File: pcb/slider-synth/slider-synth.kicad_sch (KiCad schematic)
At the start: 21 parts, among them J1 USB4105, J2 PJ-325C5-G, J3 Conn_01x02_Pin, SW1 SW_SPST, SW2 SW_SPST, U1 ESP32-S3-WROOM-2, U2 LM3940IMPX-3.3/NOPB

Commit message: update schem
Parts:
- removed J3: Conn_01x02_Pin, symbol Connector:Conn_01x02_Pin
- added C42, C44, C46, C47: 0.05μF, Capacitor_SMD:C_0805_2012Metric, symbol Device:C_Small
- added C43, C45: 250μF, Capacitor_SMD:C_0805_2012Metric, symbol Device:C_Small
- added C48, C49, C50: 0.1μF, Capacitor_SMD:C_0805_2012Metric, symbol Device:C_Small
- added D2, D3, D4, D5, D6: LED, LED_THT:LED_D5.0mm, symbol Device:LED
- added J3, J4: Conn_01x01_Pin, Connector_PinHeader_2.54mm:PinHeader_1x01_P2.54mm_Vertical, symbol Connector:Conn_01x01_Pin
- added R10, R11, R7, R8, R9: 330Ω, Resistor_SMD:R_0805_2012Metric, symbol Device:R_Small
- added R28, R29: 10Ω, Resistor_SMD:R_0805_2012Metric, symbol Device:R_Small
- added SW3: RotaryEncoder_Switch, Rotary_Encoder:RotaryEncoder_Alps_EC11E-Switch_Vertical_H20mm, symbol Device:RotaryEncoder_Switch
- added U32: MCP4922, Package_SO:SOIC-14_3.9x8.7mm_P1.27mm, symbol Analog_DAC:MCP4922
- added U33, U34: LM386, Package_SO:SOIC-8_3.9x4.9mm_P1.27mm, symbol Amplifier_Audio:LM386
- SW1, SW2: footprint (none) -> Button_Switch_THT:SW_PUSH_6mm
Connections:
- net 3v3: now also D2.2 (A)
- net 5v: now also U33.6 (V+), U34.6 (V+)
- net GND: now also J2.S, C46.2, C47.2, C48.1, C49.1, C50.1, R10.2, R11.2, R28.1, R29.1, R7.2, R8.2, R9.2, SW3.C, SW3.S2, U32.12 (Vss), U32.8 (~{LDAC}), U33.2 (-), U33.4 (GND), U34.2 (-), U34.4 (GND)
- net RX: now also J3.1 (Pin_1)
- net TX: now also J4.1 (Pin_1)
- net LED4: now reaches U1.10 (IO17)
- net LED4: now also D6.2 (A)
- net RotA: now reaches U1.15 (IO3)
- net RotA: now also SW3.A
- net CS: now reaches U1.18 (IO10)
- net CS: now also U32.3 (~{CS})
- net SDI: now reaches U1.19 (IO11)
- net SDI: now also U32.5 (SDI)
- net VDD: now reaches R4.2, U1.2 (3V3)
- net VDD: now also C50.2, U32.1 (Vdd), U32.11 (VrefB), U32.13 (VrefA), U32.9 (~{SHDN})
- net SCK: now reaches U1.20 (IO12)
- net SCK: now also U32.4 (SCK)
- net LED1: now reaches U1.22 (IO14)
- net LED1: now also D3.2 (A)
- net RotB: now reaches U1.4 (IO4)
- net RotB: now also SW3.B
- net RotSw: now reaches U1.5 (IO5)
- net RotSw: now also SW3.S1
- net LED2: now reaches U1.8 (IO15)
- net LED2: now also D4.2 (A)
- net LED3: now reaches U1.9 (IO16)
- net LED3: now also D5.2 (A)
- net R: now reaches J2.R
- net R: now also C43.2
- net T: now reaches J2.T
- net T: now also C45.2
- new net: C44.1, C45.1, U34.5
- new net: D3.1 (K), R8.1
- new net: C47.1, U34.7 (BYPASS)
- new net: C42.1, C43.1, U33.5
- new net: C42.2, R28.2
- new net: D5.1 (K), R10.1
- new net: C48.2, U32.10 (VB), U34.3 (+)
- new net: C49.2, U32.14 (VA), U33.3 (+)
- new net: C44.2, R29.2
- new net: D4.1 (K), R9.1
- new net: C46.1, U33.7 (BYPASS)
- new net: D6.1 (K), R11.1
- new net: D2.1 (K), R7.1
- no-connect marks 2 -> 6
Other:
- note added: "2x LM386 op-amp for l/r channel headphones"
- note added: "3.5mm output"
- note added: "MCP4922 DAC for turning SPI to analog audio"
- note added: "basically same above"
- note added: "boot and reset buttons"
- note added: "esp32-s3 wroom mcu"
- note added: "indicator leds"
- note added: "ldo to take 5v to 3v3"
- note added: "rotary encoder"
- note added: "usb c power delivery + coms"
- moved on the sheet: C1, C2, C3, C4, C5, C6, C7, D1, J1, J2, R1, R2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

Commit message: price optimizations
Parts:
- C3: value 33μF -> 47μF
- C42, C44: value 0.05μF -> 33nF
- C43, C45: value 250μF -> 47μF
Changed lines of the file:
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@@
 			)
 		)
-		(property "Value" "250μF"
+		(property "Value" "47μF"
 			(at 274.32 135.89 0)
 			(effects
@@
 			)
 		)
-		(property "Value" "33μF"
+		(property "Value" "47μF"
 			(at 139.7 109.2262 0)
 			(effects
@@
 		(dnp no)
 		(property "Reference" "C42"
-			(at 260.35 77.47 0)
-			(effects
-				(font
-					(size 1.27 1.27)
-				)
-				(justify left)
-			)
-		)
-		(property "Value" "0.05μF"
-			(at 260.35 80.01 0)
+			(at 262.382 77.47 0)
+			(effects
+				(font
+					(size 1.27 1.27)
+				)
+				(justify left)
+			)
+		)
+		(property "Value" "33nF"
+			(at 262.382 80.01 0)
 			(effects
 				(font
@@
 			)
 		)
-		(property "Value" "250μF"
+		(property "Value" "47μF"
 			(at 276.86 82.55 0)
 			(effects
@@
 		(dnp no)
 		(property "Reference" "C44"
-			(at 257.81 130.81 0)
-			(effects
-				(font
-					(size 1.27 1.27)
-				)
-				(justify left)
-			)
-		)
-		(property "Value" "0.05μF"
-			(at 257.81 133.35 0)
-			(effects
-				(font
+			(at 259.588 130.81 0)
+			(effects
+				(font
+					(size 1.27 1.27)
+				)
+				(justify left)
+			)
+		)
+		(property "Value" "33nF"
+			(at 259.588 133.35 0)
+			(effects
+				(font

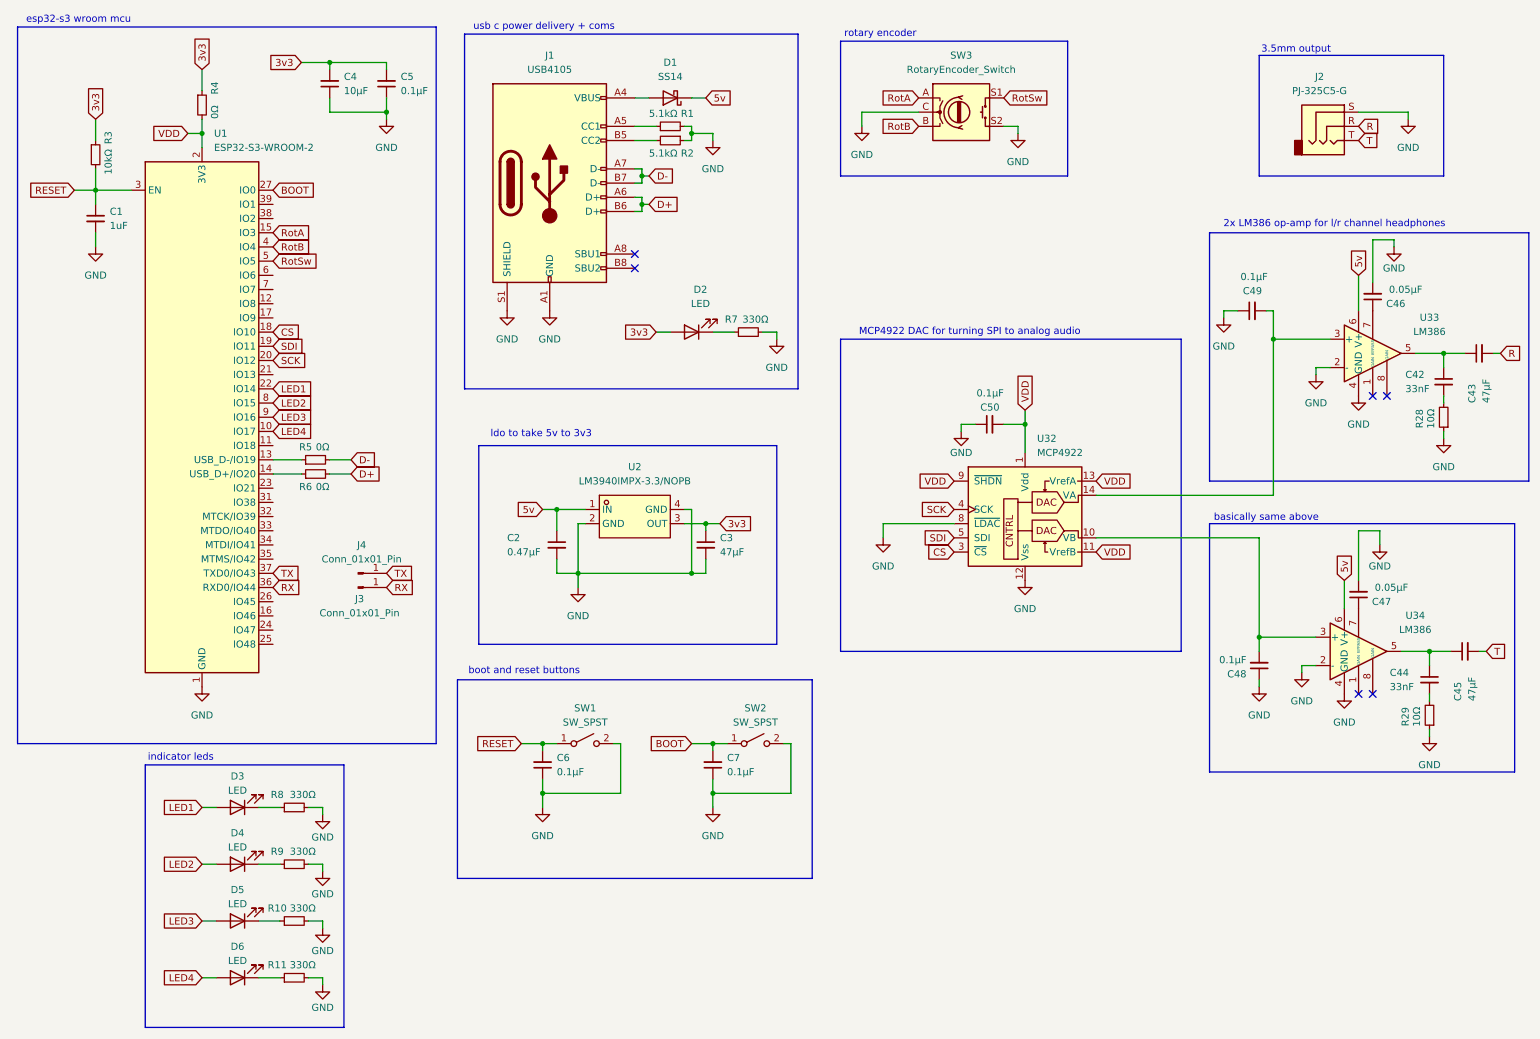
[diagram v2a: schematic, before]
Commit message: add fsr and linear pot
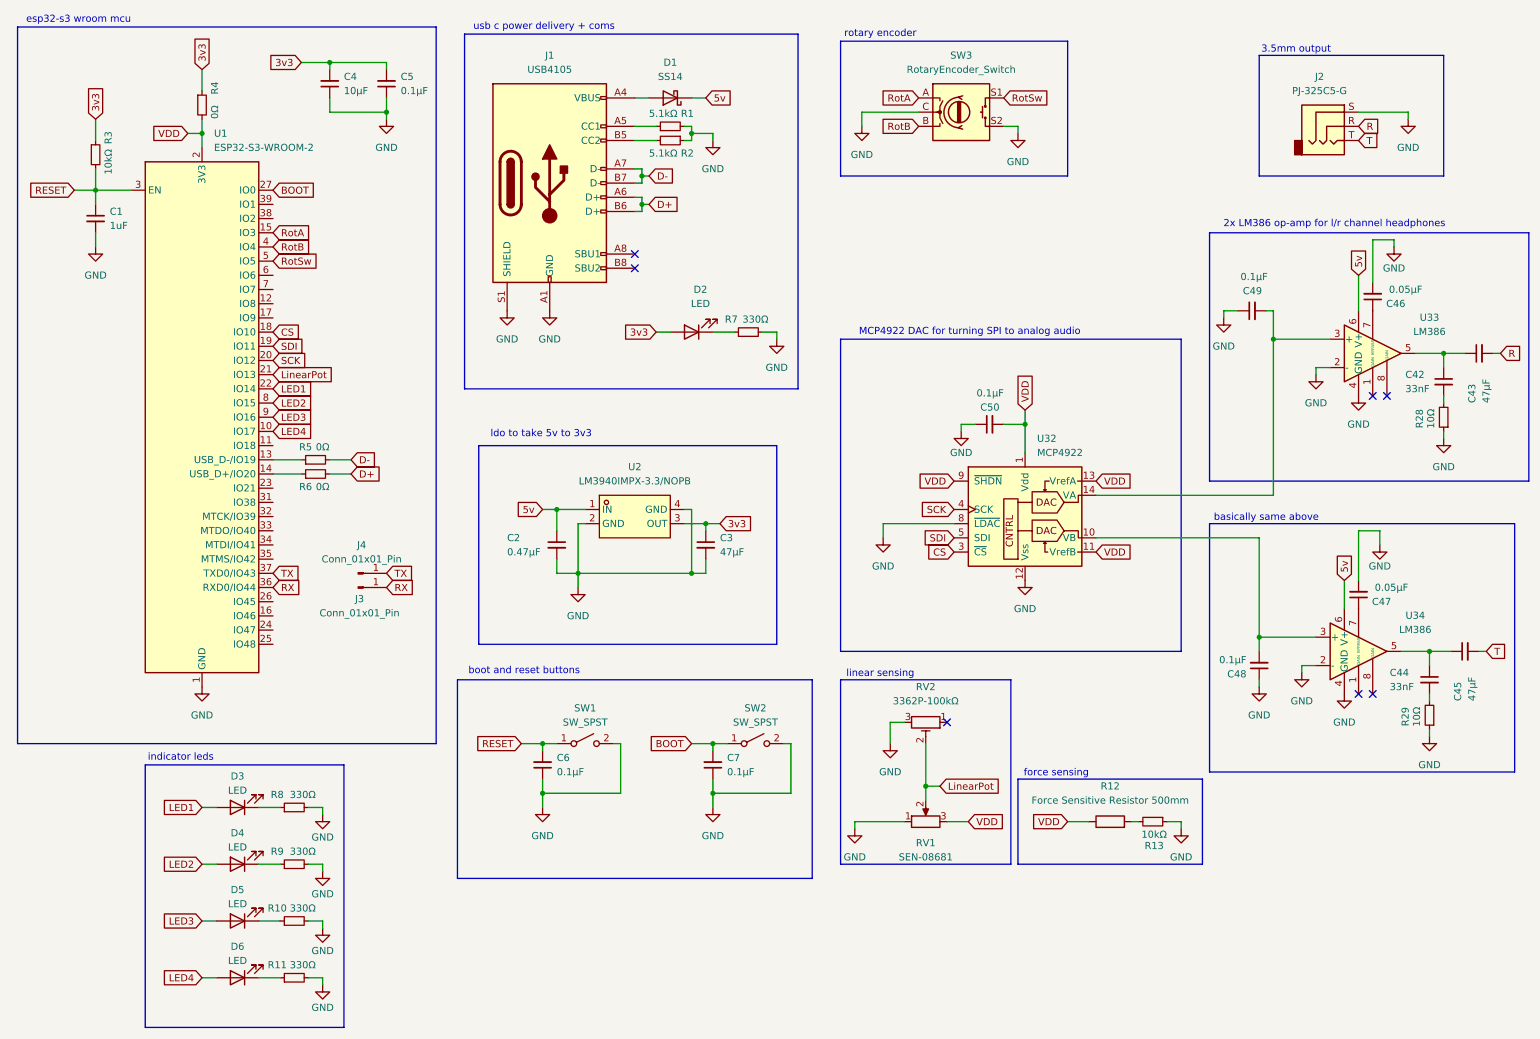
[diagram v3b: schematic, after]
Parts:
- added R12: Force Sensitive Resistor 500mm, Connector_PinSocket_2.54mm:PinSocket_1x02_P2.54mm_Vertical, symbol Device:R
- added R13: 10kΩ, Resistor_SMD:R_0805_2012Metric, symbol Device:R_Small
- added RV1: SEN-08681, Connector_PinSocket_2.54mm:PinSocket_1x03_P2.54mm_Vertical, symbol Device:R_Potentiometer
- added RV2: 3362P-100kΩ, 2_udu_lib:POT_3362P, symbol Device:R_Potentiometer_Trim
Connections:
- net GND: now also R13.1, RV1.1, RV2.3
- net VDD: now also R12.1, RV1.3
- net LinearPot: now reaches U1.21 (IO13)
- net LinearPot: now also RV1.2, RV2.2
- new net: R12.2, R13.2
- no-connect marks 6 -> 7
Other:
- note added: "force sensing"
- note added: "linear sensing"

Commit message: footprints and routing
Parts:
- removed D2: LED, LED_THT:LED_D5.0mm, symbol Device:LED
- removed R7: 330Ω, Resistor_SMD:R_0805_2012Metric, symbol Device:R_Small
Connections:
- net LED1: now also U1.32 (MTCK/IO39); no longer U1.22 (IO14)
- net LED2: now also U1.33 (MTDO/IO40); no longer U1.8 (IO15)
- net LED3: now also U1.34 (MTDI/IO41); no longer U1.9 (IO16)
- net LED4: now also U1.35 (MTMS/IO42); no longer U1.10 (IO17)
- net RotA: now also U1.23 (IO21); no longer U1.15 (IO3)
- net RotB: now also U1.24 (IO47); no longer U1.4 (IO4)
- net RotSw: now also U1.25 (IO48); no longer U1.5 (IO5)
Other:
- moved on the sheet: R5, R6

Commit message: Add bom, readme/journal stuff
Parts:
- C46, C47: value 0.05μF -> 47nF
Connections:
- net FSR: now reaches U1.31 (IO38)
- net FSR: now also R12.2, R13.2
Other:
- moved on the sheet: R12, R13
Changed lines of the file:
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@@
 	)
 	(rectangle
-		(start 193.04 149.86)
+		(start 193.04 147.32)
 		(end 226.06 165.1)
 		(stroke
@@
 	(text "force sensing\n"
 		(exclude_from_sim no)
-		(at 199.898 148.844 0)
+		(at 199.898 146.304 0)
 		(effects
 			(font
@@
 	)
 	(junction
+		(at 214.63 154.94)
+		(diameter 0)
+		(color 0 0 0 0)
+	)
+	(junction
 		(at 27.94 44.45)
 		(diameter 0)
@@
 	(wire
 		(pts
+			(xy 214.63 154.94) (xy 213.36 154.94)
+		)
+		(stroke
+			(width 0)
+			(type default)
+		)
+	)
+	(wire
+		(pts
 			(xy 24.13 44.45) (xy 27.94 44.45)
 		)
@@
 	(wire
 		(pts
-			(xy 201.93 157.48) (xy 205.74 157.48)
+			(xy 203.2 154.94) (xy 205.74 154.94)
 		)
 		(stroke
@@
 	(wire
 		(pts
+			(xy 214.63 154.94) (xy 214.63 161.29)
+		)
+		(stroke
+			(width 0)
+			(type default)
+		)
+	)
+	(wire
+		(pts
 			(xy 27.94 44.45) (xy 34.29 44.45)
 		)
@@
 	(wire
 		(pts
+			(xy 207.01 161.29) (xy 214.63 161.29)
+		)
+		(stroke
+			(width 0)
+			(type default)
+		)
+	)
+	(wire
+		(pts
 			(xy 124.46 27.94) (xy 127 27.94)
 		)
@@
 	(wire
 		(pts
-			(xy 222.25 157.48) (xy 219.71 157.48)
+			(xy 220.98 154.94) (xy 223.52 154.94)
 		)
 		(stroke
@@
 	(wire
 		(pts
-			(xy 222.25 158.75) (xy 222.25 157.48)
+			(xy 223.52 156.21) (xy 223.52 154.94)
 		)
 		(stroke
@@
 	(wire
 		(pts
-			(xy 214.63 157.48) (xy 213.36 157.48)
+			(xy 215.9 154.94) (xy 214.63 154.94)
 		)
 		(stroke
@@
 	(global_label "VDD"
 		(shape input)
-		(at 201.93 157.48 180)
+		(at 203.2 154.94 180)
 		(fields_autoplaced yes)
 		(effects
@@
 		)
 		(property "Intersheetrefs" "${INTERSHEET_REFS}"
-			(at 195.3162 157.48 0)
+			(at 196.5862 154.94 0)
 			(effects
 				(font
@@
 		)
 	)
+	(global_label "FSR"
+		(shape input)
+		(at 59.69 100.33 0)
+		(fields_autoplaced yes)
+		(effects
+			(font
+				(size 1.27 1.27)
+			)
+			(justify left)
+		)
+		(property "Intersheetrefs" "${INTERSHEET_REFS}"
+			(at 66.2433 100.33 0)
+			(effects
+				(font
+					(size 1.27 1.27)
+				)
+				(justify left)
+				(hide yes)
+			)
+		)
+	)
 	(global_label "R"
 		(shape input)
@@
 		)
 	)
+	(global_label "FSR"
+		(shape input)
+		(at 207.01 161.29 180)
+		(fields_autoplaced yes)
+		(effects
+			(font
+				(size 1.27 1.27)
+			)
+			(justify right)
+		)
+		(property "Intersheetrefs" "${INTERSHEET_REFS}"
+			(at 200.4567 161.29 0)
+			(effects
+				(font
+					(size 1.27 1.27)
+				)
+				(justify right)
+				(hide yes)
+			)
+		)
+	)
 	(global_label "BOOT"
 		(shape input)
@@
 	(symbol
 		(lib_id "Device:R_Small")
-		(at 217.17 157.48 270)
+		(at 218.44 154.94 270)
 		(unit 1)
 		(exclude_from_sim no)
@@
 		(dnp no)
 		(property "Reference" "R13"
-			(at 217.424 161.798 90)
+			(at 218.694 159.258 90)
 			(effects
 				(font
@@
 		)
 		(property "Value" "10kΩ"
-			(at 217.424 159.766 90)
+			(at 218.694 157.226 90)
 			(effects
 				(font
@@
 		)
 		(property "Footprint" "Resistor_SMD:R_0805_2012Metric"
-			(at 217.17 157.48 0)
+			(at 218.44 154.94 0)
 			(effects
 				(font
@@
 		)
 		(property "Datasheet" "~"
-			(at 217.17 157.48 0)
+			(at 218.44 154.94 0)
 			(effects
 				(font
@@
 		)
 		(property "Description" "Resistor, small symbol"
-			(at 217.17 157.48 0)
+			(at 218.44 154.94 0)
 			(effects
 				(font
@@
 			)
 		)
-		(property "Value" "0.05μF"
-			(at 262.89 115.57 0)
+		(property "Value" "47nF"
+			(at 260.858 116.078 0)
 			(effects
 				(font
@@
 	(symbol
 		(lib_id "Device:R")
-		(at 209.55 157.48 90)
+		(at 209.55 154.94 90)
 		(unit 1)
 		(exclude_from_sim no)
@@
 		(fields_autoplaced yes)
 		(property "Reference" "R12"
-			(at 209.55 151.13 90)
+			(at 209.55 148.59 90)
 			(effects
 				(font
@@
 		)
 		(property "Value" "Force Sensitive Resistor 500mm"
-			(at 209.55 153.67 90)
+			(at 209.55 151.13 90)
 			(effects
 				(font
@@
 		)
 		(property "Footprint" "Connector_PinSocket_2.54mm:PinSocket_1x02_P2.54mm_Vertical"
-			(at 209.55 159.258 90)
+			(at 209.55 156.718 90)
 			(effects
 				(font
@@
 		)
 		(property "Datasheet" "~"
-			(at 209.55 157.48 0)
+			(at 209.55 154.94 0)
 			(effects
 				(font
@@
 		)
 		(property "Description" "Resistor"
-			(at 209.55 157.48 0)
+			(at 209.55 154.94 0)
 			(effects
 				(font
@@
 			)
 		)
-		(property "Value" "0.05μF"
-			(at 265.43 62.23 0)
+		(property "Value" "47nF"
+			(at 262.89 62.23 0)
 			(effects
 				(font
@@
 	(symbol
 		(lib_id "power:GND")
-		(at 222.25 158.75 0)
+		(at 223.52 156.21 0)
 		(unit 1)
 		(exclude_from_sim no)
@@
 		(fields_autoplaced yes)
 		(property "Reference" "#PWR020"
-			(at 222.25 165.1 0)
+			(at 223.52 162.56 0)
 			(effects
 				(font
@@
 		)
 		(property "Value" "GND"
-			(at 222.25 163.83 0)
+			(at 223.52 161.29 0)
 			(effects
 				(font
@@
 		)
 		(property "Footprint" ""
-			(at 222.25 158.75 0)
+			(at 223.52 156.21 0)
 			(effects
 				(font
@@
 		)
 		(property "Datasheet" ""
-			(at 222.25 158.75 0)
+			(at 223.52 156.21 0)
 			(effects
 				(font
@@
 		)
 		(property "Description" "Power symbol creates a global label with name \"GND\" , ground"
-			(at 222.25 158.75 0)
+			(at 223.52 156.21 0)
 			(effects
 				(font

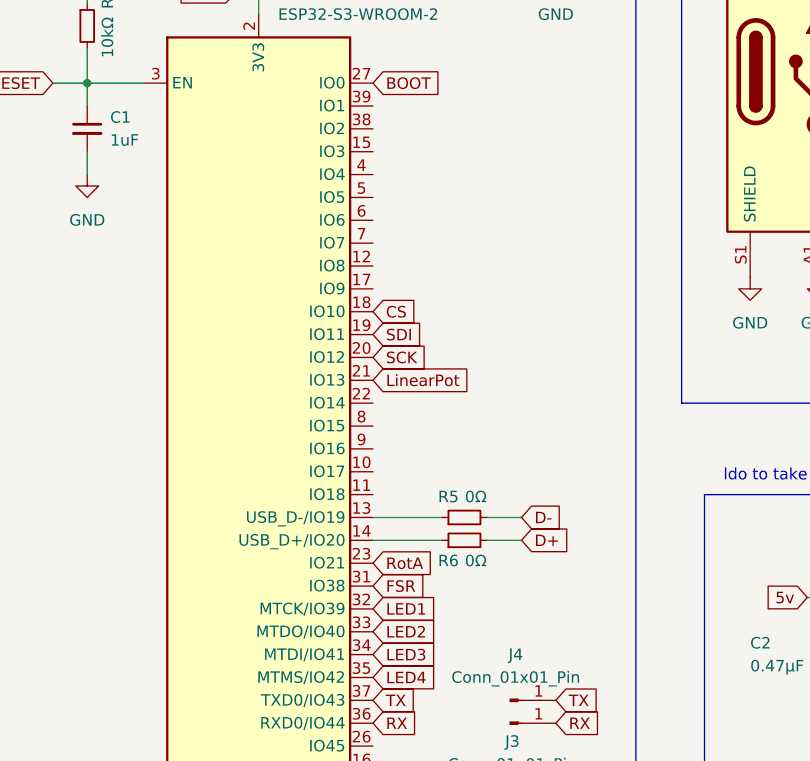
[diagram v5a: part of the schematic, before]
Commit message: move io38 to io4, but did not update prod files
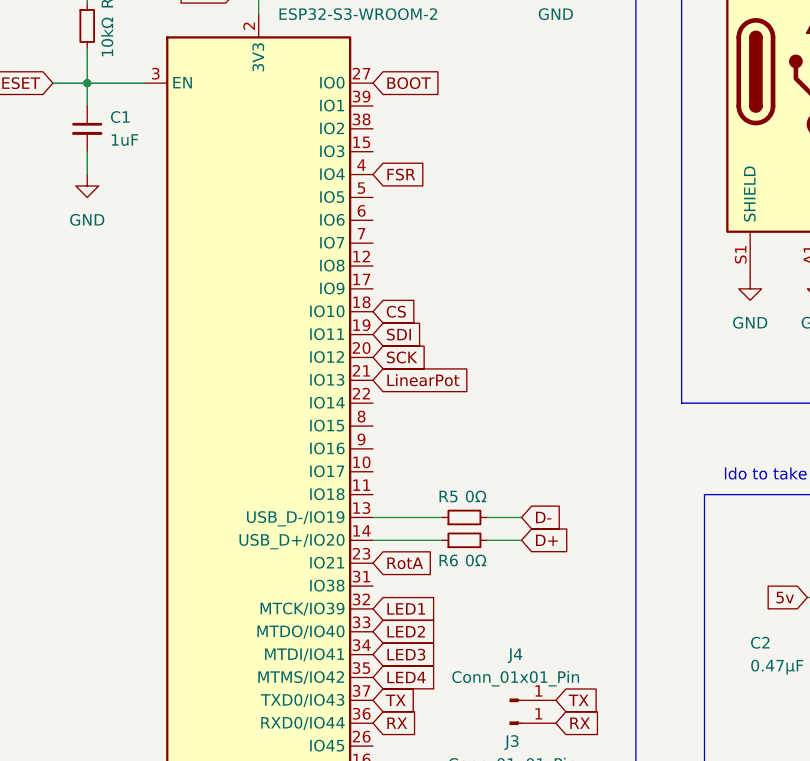
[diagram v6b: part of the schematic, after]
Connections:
- net FSR: now also U1.4 (IO4); no longer U1.31 (IO38)
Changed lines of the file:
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@@
+		)
+	)
+	(global_label "FSR"
+		(shape input)
+		(at 59.69 54.61 0)
+		(fields_autoplaced yes)
+		(effects
+			(font
+				(size 1.27 1.27)
+			)
+			(justify left)
+		)
+		(property "Intersheetrefs" "${INTERSHEET_REFS}"
+			(at 66.2433 54.61 0)
+			(effects
+				(font
+					(size 1.27 1.27)
+				)
+				(justify left)
+				(hide yes)
+			)
 		)
 	)
@@
 			(effects
 				(font
-					(size 1.27 1.27)
-				)
-				(justify left)
-				(hide yes)
-			)
-		)
-	)
-	(global_label "FSR"
-		(shape input)
-		(at 59.69 100.33 0)
-		(fields_autoplaced yes)
-		(effects
-			(font
-				(size 1.27 1.27)
-			)
-			(justify left)
-		)
-		(property "Intersheetrefs" "${INTERSHEET_REFS}"
-			(at 66.2433 100.33 0)
-			(effects
-				(font
